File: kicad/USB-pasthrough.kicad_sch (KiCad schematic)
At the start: 96 parts, among them J1 USB_Power, J10 SD-1-A, J2 USB_C, J3 Cortex Debug, J4 Power_Sel, J5 SPI Display, J6 SWD, J7 USB_A, J8 MicroSD, J9 Serial, SW1 Boot0, SW2 Reset, U1 AMS1117, U2 STM32F723VET6, Y1 8 MHz

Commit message: First Pass v0.2 schematic
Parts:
- removed C12, C17, C20, C4: 4.7uF, Capacitor_SMD:C_0805_2012Metric_Pad1.18x1.45mm_HandSolder, symbol Device:C
- removed TP11: V12PHYHS, TestPoint:TestPoint_Pad_D1.0mm, symbol Connector:TestPoint
- added C14, C15, C23, C5: 4.7uF, Capacitor_SMD:C_0603_1608Metric_Pad1.08x0.95mm_HandSolder, symbol Device:C
- added TP9: V12PHYHS, TestPoint:TestPoint_Pad_D1.0mm, symbol Connector:TestPoint
- C9: renamed from C5; footprint Capacitor_SMD:C_0805_2012Metric_Pad1.18x1.45mm_HandSolder -> Capacitor_SMD:C_0603_1608Metric_Pad1.08x0.95mm_HandSolder
- TP12: value USBA+ -> USBA-
- TP13: value USBA- -> USBA+
- gave numbers to parts that had none: 6
- renumbered C11 to C1, C8 to C10, C13 to C11, C10 to C12, C9 to C13, C18 to C16, C14 to C17, C15 to C18, C16 to C19, C3 to C2, C22 to C20, C25 to C21, C23 to C22, C21 to C25, C1 to C3, C19 to C4, C7 to C6, C6 to C7, C2 to C8, J4 to J1, J8 to J10, J1 to J2, J2 to J3, J3 to J4, J9 to J7, J7 to J8, J10 to J9, LED3 to LED2, LED4 to LED3, LED2 to LED4, R2 to R1, R7 to R10, R10 to R12, R12 to R13, R13 to R14, R9 to R16, R14 to R18, R20 to R19, R1 to R2, R18 to R20, R19 to R21, R23 to R22, R21 to R23, R22 to R24, R6 to R5, R5 to R6, R16 to R7, R8 to R9, TP9 to TP11
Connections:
- net +3V3: now also C9.2, C14.1, C15.2, C23.1, C5.2
- net GND: now also C10.2, C17.1, C2.1, C22.2, C6.1, ID1.2 (B), ID2.2 (B), ID3.2 (B), ID4.2 (B), ID5.2 (B), C14.2, C15.1, C23.2, C5.1
- net USBA+: now also TP13.1; no longer TP12.1
- net USBA-: now also TP12.1; no longer TP13.1
- net V12PHYHS: now also TP9.1
- net at ID3.1 (A): now also U2.88 (PD7); no longer U2.62 (PD15)
- net at U2.58 (PD11): no longer ID1.1 (A)
- net at U2.59 (PD12): no longer ID5.1 (A)
- net at U2.60 (PD13): no longer ID2.1 (A)
- net at U2.61 (PD14): no longer ID4.1 (A)
- net at U2.84 (PD3): now also ID1.1 (A)
- net at U2.85 (PD4): now also ID5.1 (A)
- net at U2.86 (PD5): now also ID2.1 (A)
- net at U2.87 (PD6): now also ID4.1 (A)
- no-connect marks 46 -> 47
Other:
- moved on the sheet: C11, C9, ID1, ID2, ID3, ID4, ID5, J10, LED2, LED3, LED4, R22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

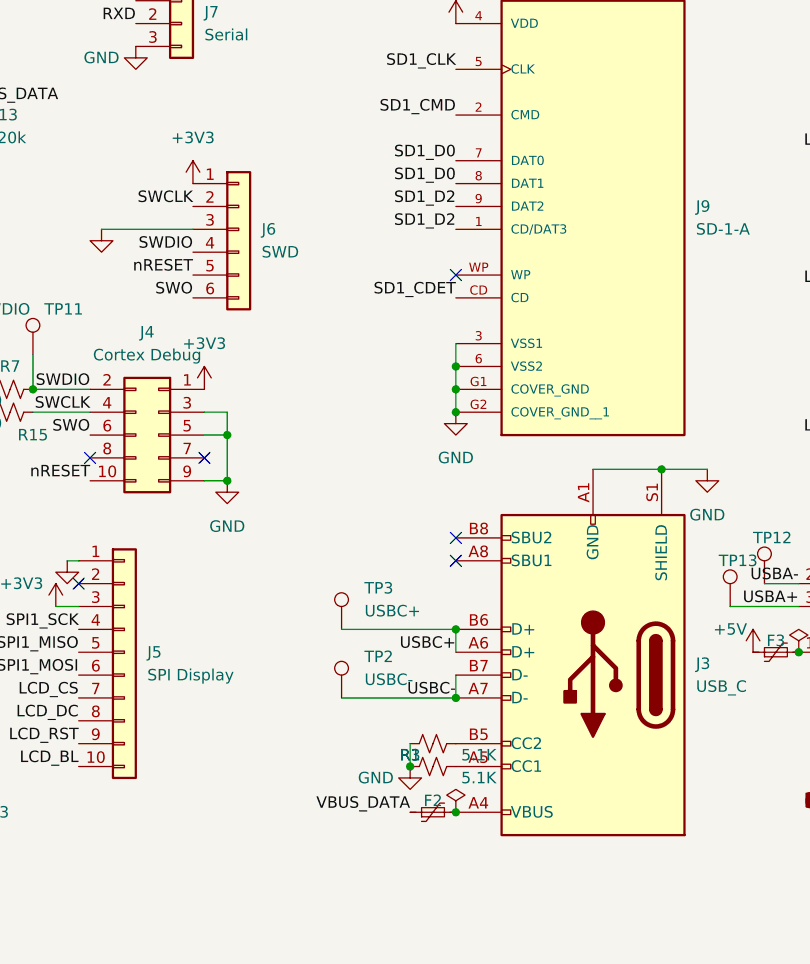
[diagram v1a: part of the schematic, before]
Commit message: Test routing, many courtyard conflicts
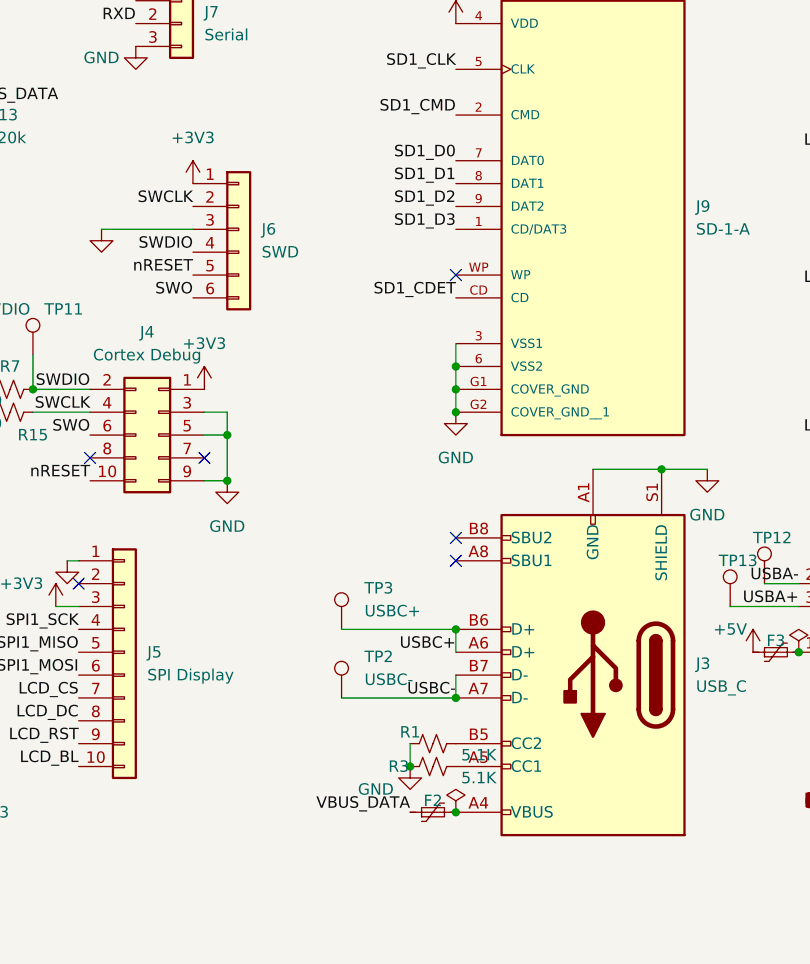
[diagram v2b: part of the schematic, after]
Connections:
- net SD1_D0: no longer J9.8 (DAT1)
- net SD1_D1: now also J9.8 (DAT1)
- net SD1_D2: no longer J9.1 (CD/DAT3)
- net SD1_D3: now also J9.1 (CD/DAT3)
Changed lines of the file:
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@@
-    (effects (font (size 1.27 1.27)) (justify right bottom))
-  )
-  (label "SD1_D0" (at 207.01 92.71 180)
     (effects (font (size 1.27 1.27)) (justify right bottom))
   )
@@
     (effects (font (size 1.27 1.27)) (justify right bottom))
   )
-  (label "SD1_D2" (at 207.01 97.79 180)
-    (effects (font (size 1.27 1.27)) (justify right bottom))
-  )
   (label "VCAP_1" (at 80.01 170.18 180)
     (effects (font (size 1.27 1.27)) (justify right bottom))
@@
     (effects (font (size 1.27 1.27)) (justify right bottom))
   )
+  (label "SD1_D3" (at 207.01 97.79 180)
+    (effects (font (size 1.27 1.27)) (justify right bottom))
+  )
   (label "LCD_BL" (at 132.08 99.06 0)
     (effects (font (size 1.27 1.27)) (justify left bottom))
@@
   )
   (label "SWCLK_" (at 154.94 118.11 180)
+    (effects (font (size 1.27 1.27)) (justify right bottom))
+  )
+  (label "SD1_D1" (at 207.01 92.71 180)
     (effects (font (size 1.27 1.27)) (justify right bottom))
   )
@@
   (symbol (lib_id "Device:R_Small_US") (at 204.47 157.48 270) (unit 1)
     (in_bom yes) (on_board yes)
-    (property "Reference" "R3" (id 0) (at 201.93 156.21 90))
+    (property "Reference" "R3" (id 0) (at 200.66 157.48 90))
     (property "Value" "5.1K" (id 1) (at 209.55 158.75 90))
     (property "Footprint" "Resistor_SMD:R_0603_1608Metric_Pad0.98x0.95mm_HandSolder" (id 2) (at 204.47 157.48 0)
@@
       (effects (font (size 1.27 1.27)) hide)
     )
-    (property "Value" "GND" (id 1) (at 198.12 158.75 0))
+    (property "Value" "GND" (id 1) (at 198.12 160.02 0))
     (property "Footprint" "" (id 2) (at 201.93 157.48 0)
       (effects (font (size 1.27 1.27)) hide)
@@
   (symbol (lib_id "Device:R_Small_US") (at 204.47 154.94 270) (unit 1)
     (in_bom yes) (on_board yes)
-    (property "Reference" "R1" (id 0) (at 201.93 156.21 90))
+    (property "Reference" "R1" (id 0) (at 201.93 153.67 90))
     (property "Value" "5.1K" (id 1) (at 209.55 156.21 90))
     (property "Footprint" "Resistor_SMD:R_0603_1608Metric_Pad0.98x0.95mm_HandSolder" (id 2) (at 204.47 154.94 0)

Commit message: V0.2 layout pending bring-up
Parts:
- renumbered C6 to C1, C13 to C10, C14 to C11, C1 to C12, C12 to C13, C11 to C14, C17 to C15, C15 to C16, C16 to C17, C19 to C18, C18 to C19, C7 to C2, C22 to C20, C20 to C21, C25 to C22, C24 to C23, C21 to C24, C23 to C25, C2 to C3, C5 to C4, C3 to C5, C4 to C6, C8 to C7, C9 to C8, C10 to C9, ID5 to ID2, ID2 to ID3, ID3 to ID5, J2 to J1, J3 to J2, J1 to J3, R2 to R1, R15 to R10, R12 to R11, R8 to R12, R14 to R13, R10 to R14, R7 to R15, R18 to R16, R16 to R17, R17 to R18, R21 to R19, R1 to R2, R19 to R20, R20 to R21, R23 to R22, R22 to R23, R9 to R3, R13 to R4, R4 to R5, R3 to R6, R5 to R7, R6 to R8, R11 to R9, TP5 to TP3, TP3 to TP4, TP4 to TP5, TP7 to TP6, TP6 to TP7
